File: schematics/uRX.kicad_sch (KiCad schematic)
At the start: 100 parts, among them J1 RF_In, J2 USB_C_Receptacle_USB2.0_14P, J3 AudioJack2_Ground, J4 +5Vfiltered, J5 +5V, J7 +3.3Vfiltered, J8 RF_In, Q1 BC847, U1 CBT3253, U10 IP2326, U2 LM4562, U3 ESP32-DEVKIT, U4 Si5351A-B-GT, U5 OPA2690, U6 Si4732-A10, U7 PCM1808PWR, U8 LM4040-2.5, U9 PCM1808PWR, Y1 25MHz, Y2 32768kHz

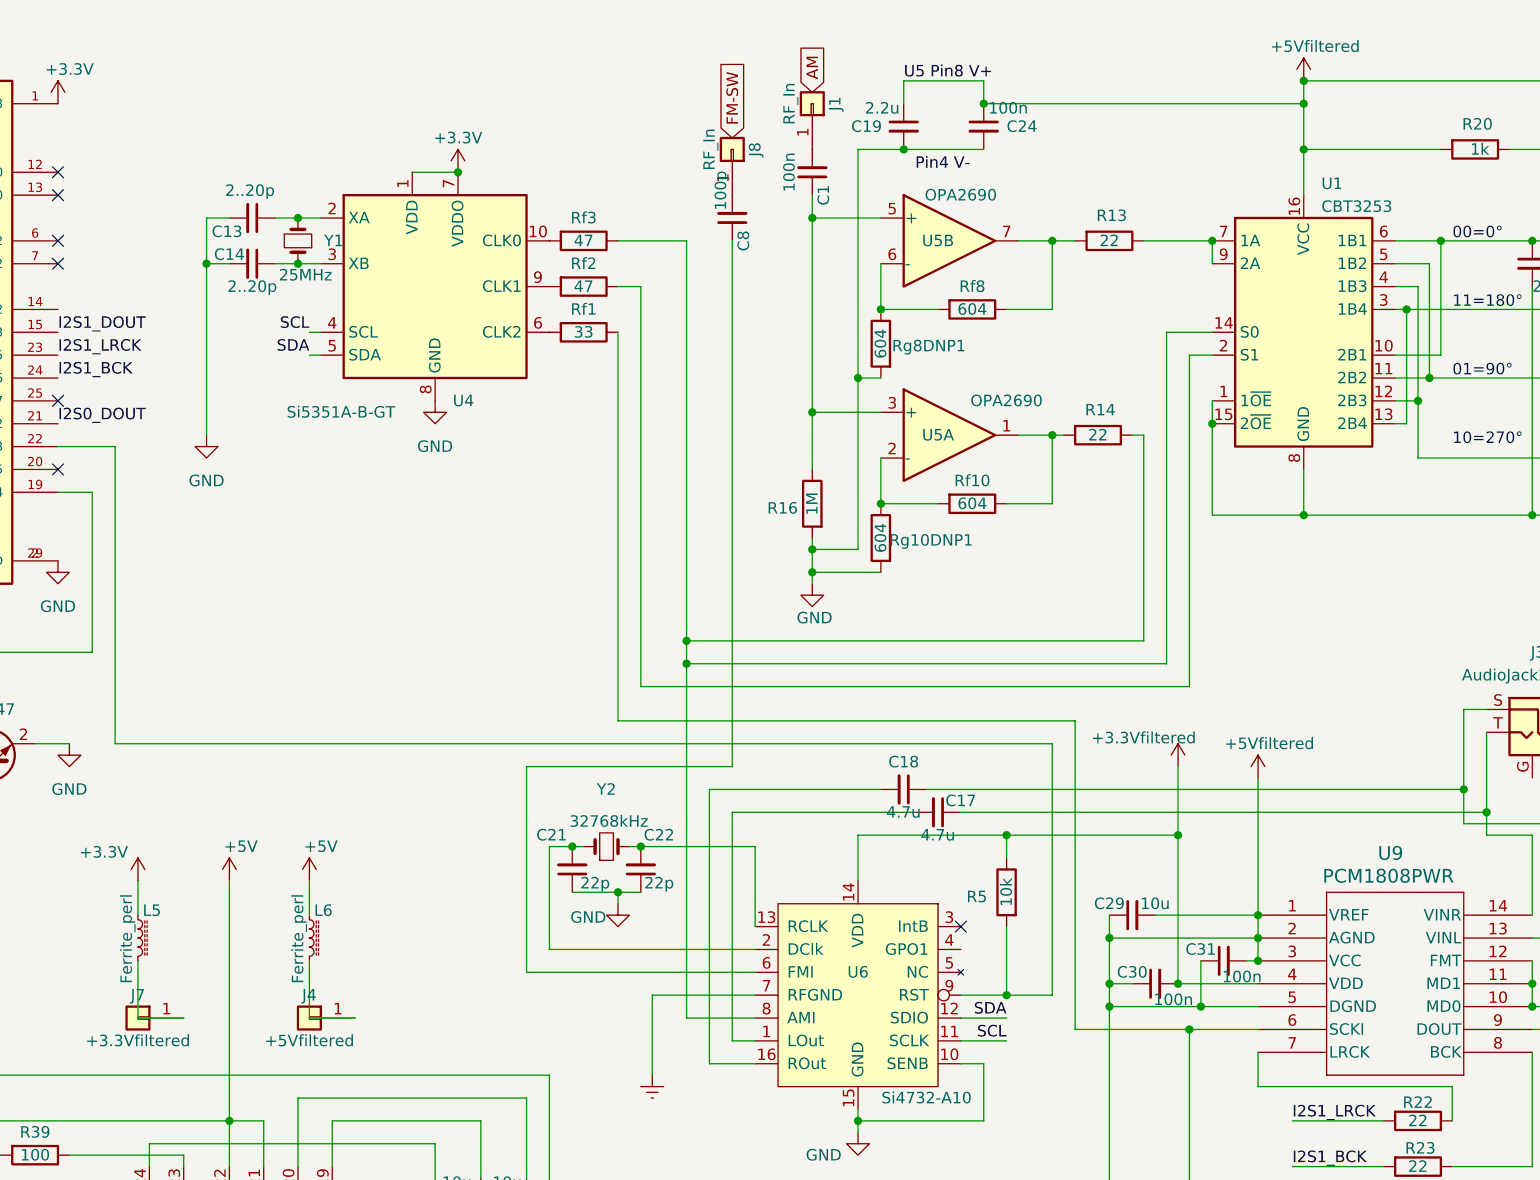
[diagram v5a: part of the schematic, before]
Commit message: use opa2211 in AM Antenna input
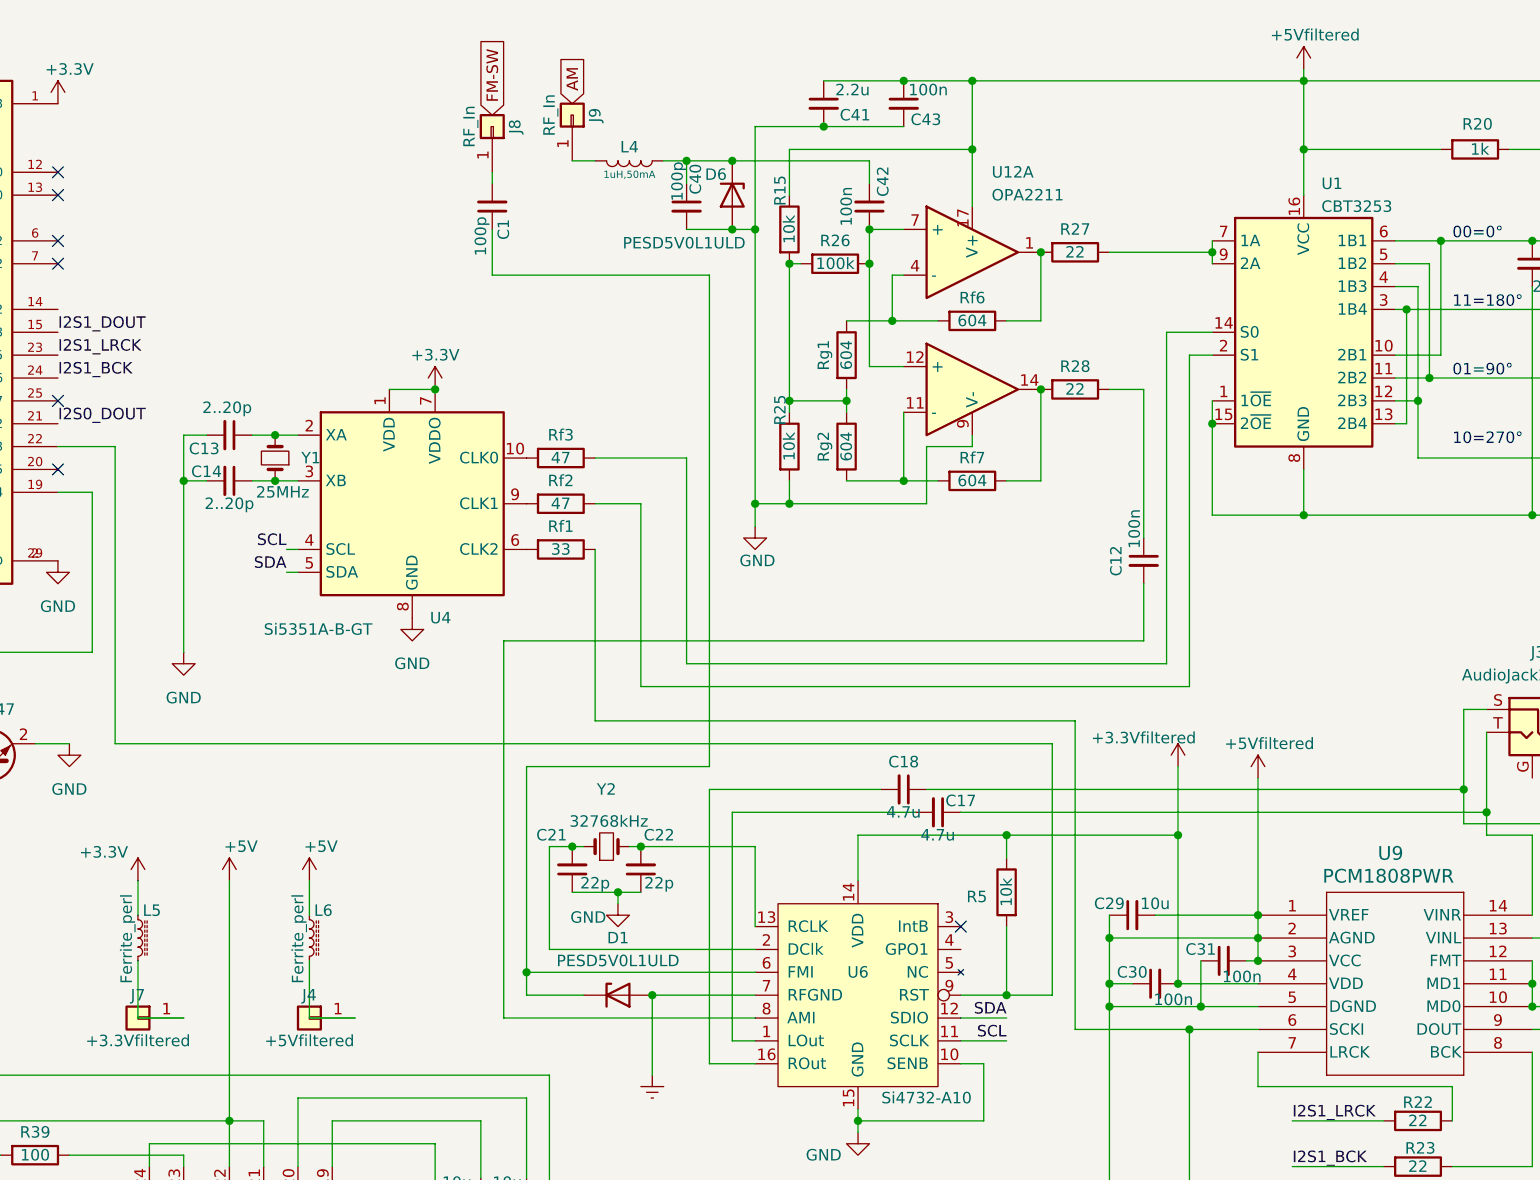
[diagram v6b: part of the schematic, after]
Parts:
- removed C19: 2.2u, Capacitor_SMD:C_0603_1608Metric, symbol Device:C_Small
- removed C24: 100n, Capacitor_SMD:C_0603_1608Metric, symbol Device:C_Small
- removed C8: 100p, Capacitor_SMD:C_0603_1608Metric, symbol Device:C_Small
- removed J1: RF_In, Connector_Pin:Pin_D0.9mm_L10.0mm_W2.4mm_FlatFork, symbol Connector_Generic:Conn_01x01
- removed R13, R14: 22, Resistor_SMD:R_0603_1608Metric, symbol Device:R
- removed R16: 1M, Resistor_SMD:R_0603_1608Metric, symbol Device:R
- removed Rf10, Rf8: 604, Resistor_SMD:R_0603_1608Metric, symbol Device:R
- removed Rg10DNP1, Rg8DNP1: 604, Resistor_THT:R_Axial_DIN0207_L6.3mm_D2.5mm_P10.16mm_Horizontal, symbol Device:R
- removed U5: OPA2690, SOIC-8, symbol Amplifier_Operational:LM4562
- added C12, C42, C43: 100n, Capacitor_SMD:C_0603_1608Metric, symbol Device:C_Small
- added C40: 100p, Capacitor_SMD:C_0603_1608Metric, symbol Device:C_Small
- added C41: 2.2u, Capacitor_SMD:C_0603_1608Metric, symbol Device:C_Small
- added D1, D6: PESD5V0L1ULD, Diode_SMD:D_SOD-882D, symbol Diode:PESD5V0L1ULD
- added J9: RF_In, Connector_Pin:Pin_D0.9mm_L10.0mm_W2.4mm_FlatFork, symbol Connector_Generic:Conn_01x01
- added L4: 1uH,50mA, PCM_JLCPCB:L_0805, symbol PCM_JLCPCB-Inductors:1uH,50mA
- added R15, R25: 10k, Resistor_SMD:R_0603_1608Metric, symbol Device:R
- added R26: 100k, Resistor_SMD:R_0603_1608Metric, symbol Device:R
- added R27, R28: 22, Resistor_SMD:R_0603_1608Metric, symbol Device:R
- added Rf6, Rf7, Rg1, Rg2: 604, Resistor_SMD:R_0603_1608Metric, symbol Device:R
- added U12: OPA2211, HTSSOP(PWP), symbol opa2211:OPA2211
- C1: value 100n -> 100p
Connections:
- net +5Vfiltered: now also C40.2, C41.1, C41.2, C43.1, C43.2, D6.2 (A), R15.1, R25.2, U12.17 (V+), U12.9 (V-)
- net Earth: now also D1.2 (A)
- net at C1.2: now also J8.1 (Pin_1)
- net at C1.1: now also U6.6 (FMI), D1.1 (K)
- net at U1.7 (1A), U1.9 (2A): now also R27.1
- net at Rf3.1, U1.14 (S0): no longer U6.8 (AMI)
- new net: C42.1, R26.1, U12.12 (+), U12.7 (+)
- new net: C40.1, C42.2, D6.1 (K), L4.1
- new net: R15.2, R25.1, R26.2, Rg1.2, Rg2.1
- new net: C12.1, R28.1
- new net: C12.2, U6.8 (AMI)
- new net: Rf7.2, Rg2.2, U12.11 (-)
- new net: R27.2, Rf6.1, U12.1
- new net: Rf6.2, Rg1.1, U12.4 (-)
- new net: R28.2, Rf7.1, U12.14
- new net: J9.1 (Pin_1), L4.2
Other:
- moved on the sheet: C13, C14, J8, Rf1, Rf2, Rf3, U4, Y1
